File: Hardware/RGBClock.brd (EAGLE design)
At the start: 81.3 x 81.3 mm, 89 parts, among them IC1 PTH08080W, IC2 LP2985-Digital, IC3 LP2985-Analog, IC4 MCP1824S, IC5 PTH08080W, Q1 MS5V, T1 IRF7205, T2 SI2323, T3 PUMH*, X1 NEB21R, X2 MICRO-SD3

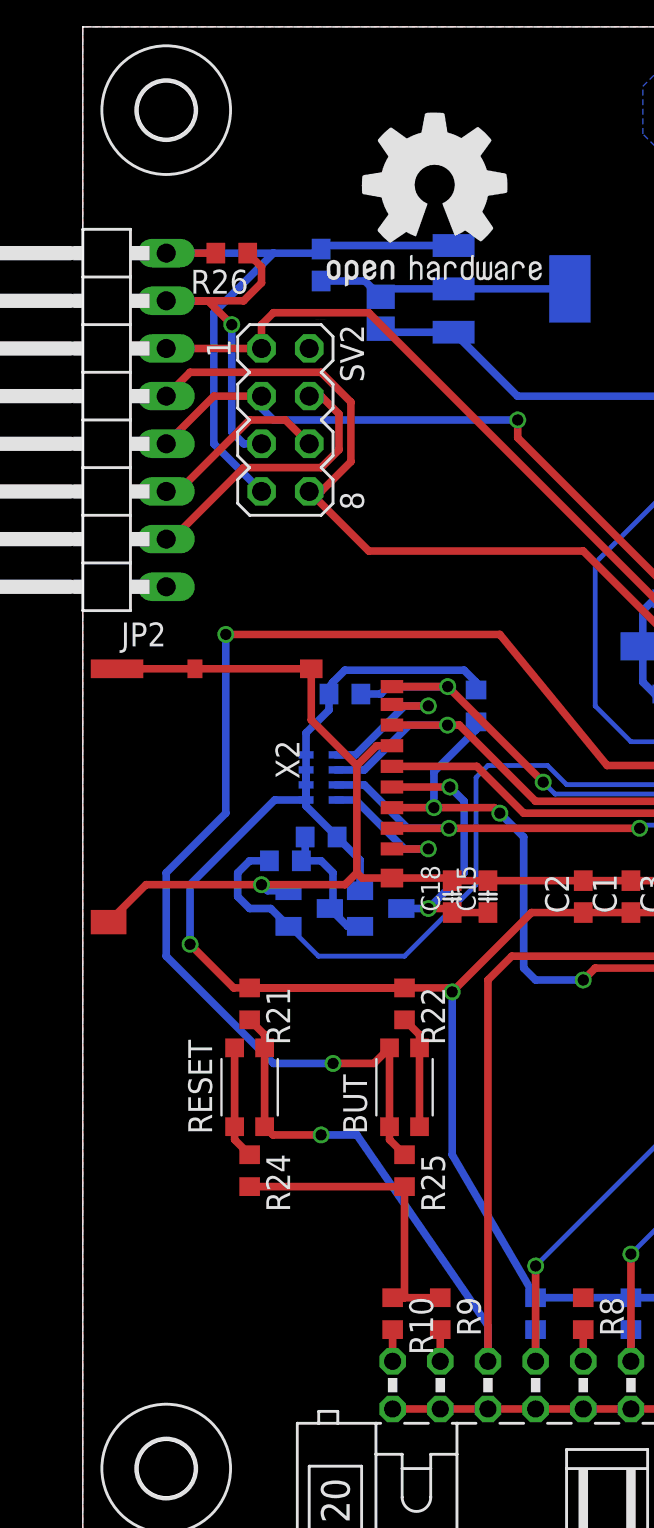
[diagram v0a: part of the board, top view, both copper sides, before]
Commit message: added github url on PCB
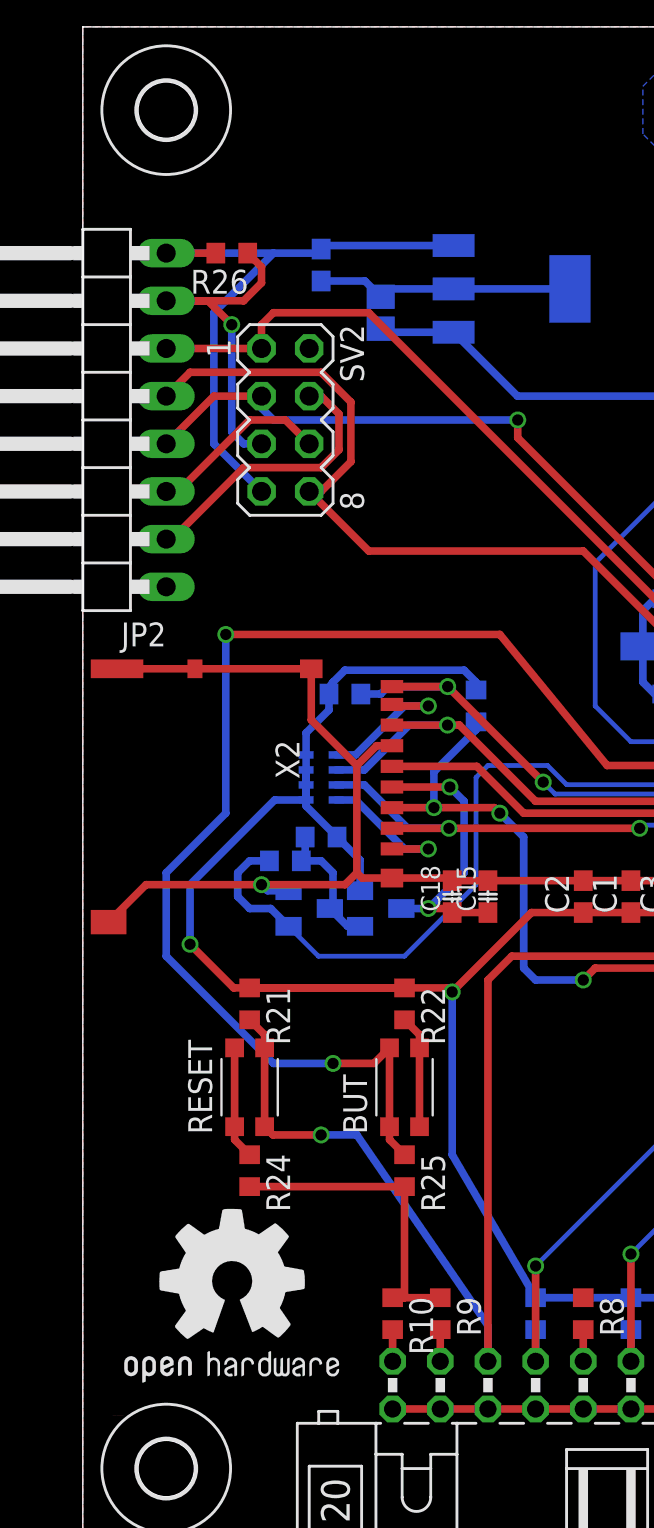
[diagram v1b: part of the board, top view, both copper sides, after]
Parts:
- moved GOLD_ORB_SM1 59.4 mm to (1.59, 7.30)
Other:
- board text added: "https://github.com/matthiasb85/RGB-Clock"
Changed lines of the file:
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@@
 <rectangle x1="6.985" y1="53.34" x2="29.845" y2="67.31" layer="51"/>
 <rectangle x1="53.975" y1="59.69" x2="67.945" y2="76.2" layer="51"/>
-<text x="11.43" y="77.47" size="1.27" layer="51" font="vector" ratio="16" distance="26">RGB Clock v0.1
+<text x="9.2075" y="73.9775" size="1.4224" layer="51" font="vector" ratio="16" distance="26">RGB Clock v0.1
 M.B. 11.2014</text>
+<text x="9.2075" y="72.0725" size="0.6096" layer="51" font="vector" ratio="16" distance="26">https://github.com/matthiasb85/RGB-Clock</text>
 </plain>
 <attributes>
@@
 <attribute name="DIGIKEY-PN" value="513-1457-1-ND" x="36.83" y="59.69" size="1.778" layer="27" rot="R270" display="off"/>
 </element>
-<element name="GOLD_ORB_SM1" library="bfl" package="OSHW1" value="OSHWLOGO_GOLD_ORB_MED" x="12.3825" y="65.7225"/>
+<element name="GOLD_ORB_SM1" library="bfl" package="OSHW1" value="OSHWLOGO_GOLD_ORB_MED" x="1.5875" y="7.3025"/>
 <element name="JP6" library="pinhead" package="1X14/90" value="" x="80.645" y="53.34" rot="R270"/>
 <element name="JP1" library="pinhead" package="1X03/90" value="" x="40.64" y="80.645"/>

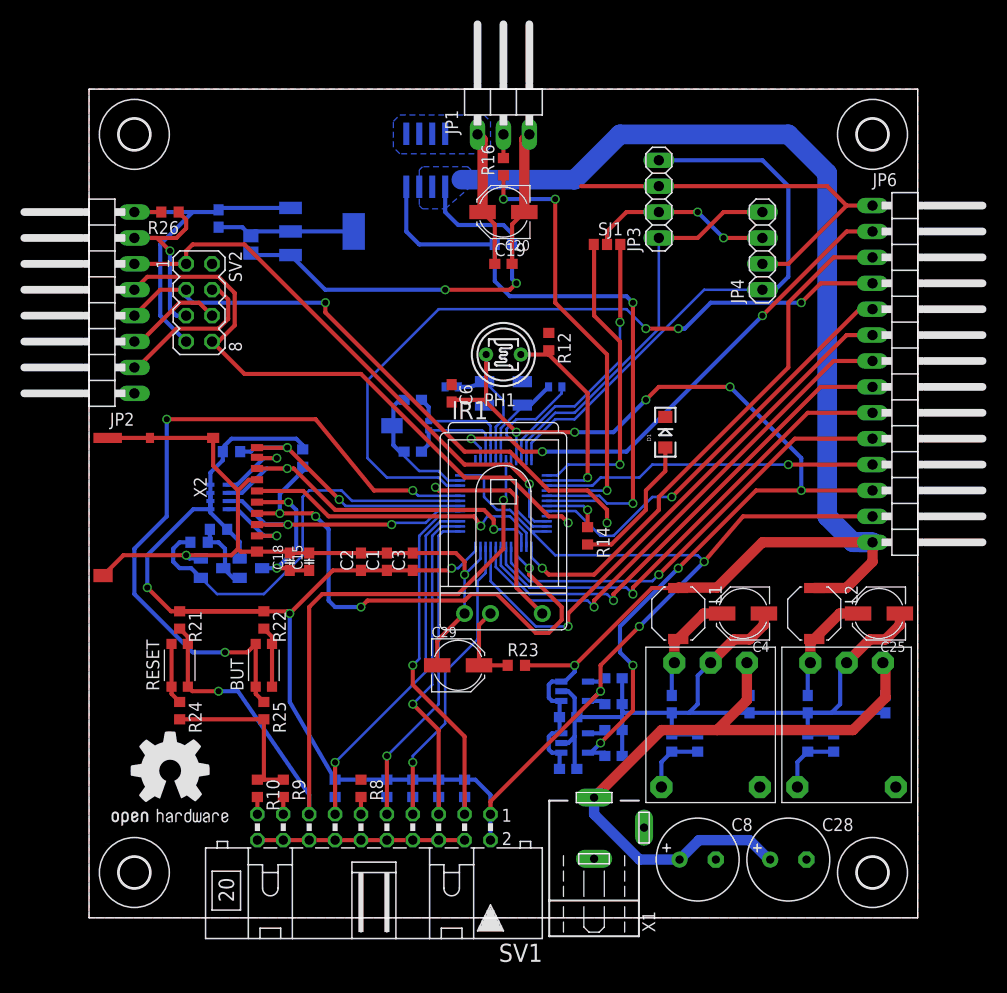
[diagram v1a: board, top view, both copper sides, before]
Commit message: worked on board worked on silkscreen -> first version should be ready within a few commits
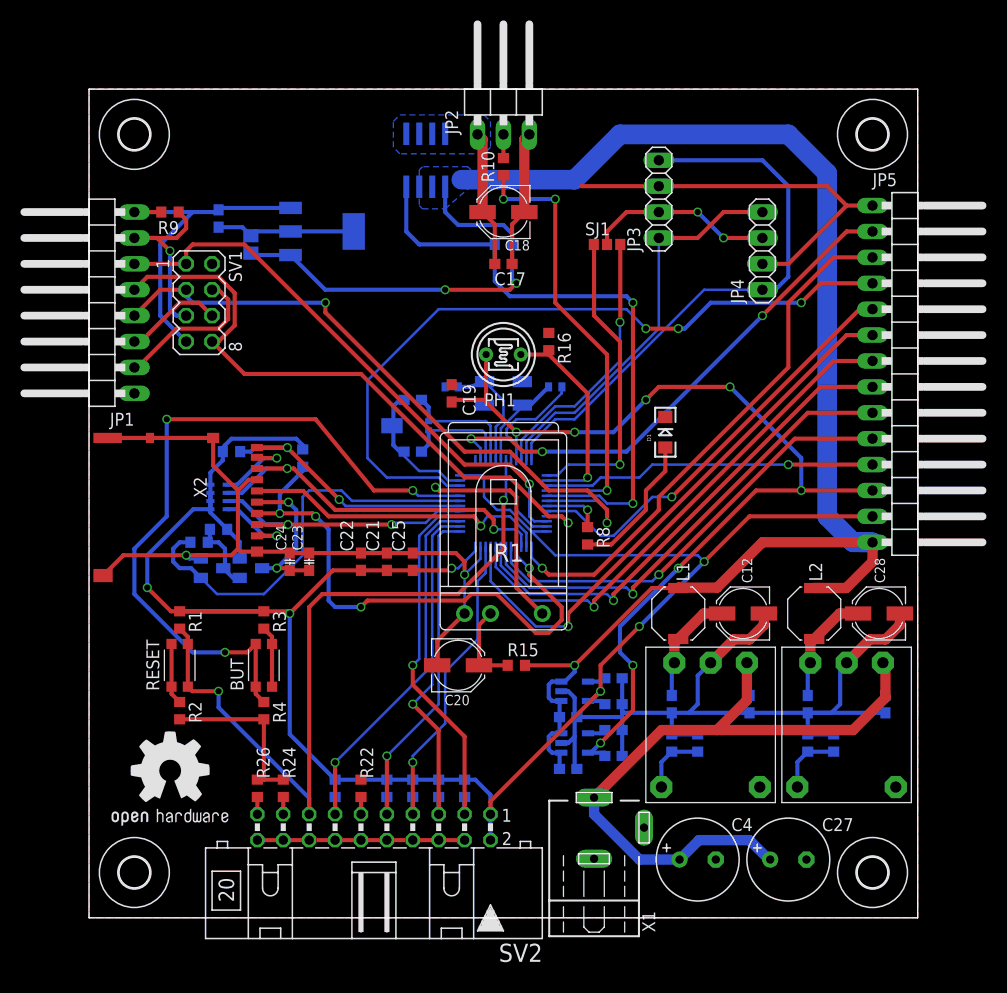
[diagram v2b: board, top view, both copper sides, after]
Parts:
- C1: value 1uF -> 18pF; device rcl:C0603 -> SparkFun:C0402
- C10: value 2u2/16V -> 10n
- C12: value 4,7u/10V -> 100µ/6V3; device 00ralf:C0603-DASHES -> rcl:PANASONIC_C
- C14: value 10n -> 2u2/16V
- C15: value 10u/6V3 -> 2µ2/16V; device 00ralf:C0603-DASHES -> rcl:C0603
- C16: value 10µ/16V -> 100n; device rcl:C0805 -> rcl:C0603
- C17: value 2µ2/16V -> 100n
- C18: value 100n -> 100µ/6V3; device 00ralf:C0603-DASHES -> rcl:PANASONIC_C
- C19: value 100n -> 1uF
- C2: value 1uF -> 100n
- C21, C22: value 18pF -> 1uF; device SparkFun:C0402 -> rcl:C0603
- C23: value 12p -> 10u/6V3; device rcl:C0603 -> 00ralf:C0603-DASHES
- C24: value 12p -> 100n; device rcl:C0603 -> 00ralf:C0603-DASHES
- C25: value 100µ/6V3 -> 12p; device rcl:PANASONIC_C -> rcl:C0603
- C27: value 100n -> 220µ; device rcl:C0603 -> rcl:E3,5-8
- C28: value 220µ -> 100µ/6V3; device rcl:E3,5-8 -> rcl:PANASONIC_C
- C29: value 100µ/6V3 -> 100n; device rcl:PANASONIC_C -> rcl:C0603
- C3: value 12p -> 18pF; device rcl:C0603 -> SparkFun:C0402
- C4: value 100µ/6V3 -> 220µ; device rcl:PANASONIC_C -> rcl:E3,5-8
- C5: value 100n -> 12p
- C6: value 1uF -> 4,7u/10V; device rcl:C0603 -> 00ralf:C0603-DASHES
- C7: value 100n -> 4,7u/10V; device rcl:C0603 -> 00ralf:C0603-DASHES
- C8: value 220µ -> 12p; device rcl:E3,5-8 -> rcl:C0603
- C9: value 4,7u/10V -> 10µ/16V; device 00ralf:C0603-DASHES -> rcl:C0805
- JP1: device pinhead:1X03/90 -> pinhead:1X08/90
- JP2: device pinhead:1X08/90 -> pinhead:1X03/90
- R10: value 10k -> 120
- R11: value 100k -> 22k; device rcl:R0603 -> 00ralf:R0603-DASHES
- R12: value 220k -> 22k; device rcl:R0603 -> 00ralf:R0603-DASHES
- R14: value 1k -> *; device rcl:R0603 -> 00ralf:R0603-DASHES
- R15: value * -> 330; device 00ralf:R0603-DASHES -> rcl:R0603
- R16: value 120 -> 220k
- R17: value 22k -> 180; device 00ralf:R0603-DASHES -> rcl:R0603
- R18: value 22k -> 330; device 00ralf:R0603-DASHES -> rcl:R0603
- R19: value 180 -> 10k
- R2, R3, R8: value 10k -> 1k
- R20, R23: value 330 -> 10k
- R22, R24: value 1k -> 10k
- R5: value 10k -> 100k
- SV1: device con-harting-ml:ML20L -> con-lstb:MA04-2
- SV2: device con-lstb:MA04-2 -> con-harting-ml:ML20L
- T2: value SI2323 -> PUMH*; device transistor-fet:SOT23 -> transistor-digital:SOT23
- T3: value PUMH* -> SI2323; device transistor-digital:SOT23 -> transistor-fet:SOT23
- moved R10 65.6 mm to (40.6, 73.7), turned to 90 degrees
- moved R18 63.3 mm to (70.5, 17.1), turned to 90 degrees
- moved C16 61.1 mm to (57.1, 21.0), turned to 270 degrees
- moved R17 59.1 mm to (73.0, 17.1)
- moved R9 57.6 mm to (7.94, 69.2), turned to 180 degrees
- moved R26 57.2 mm to (16.5, 12.7), turned to 270 degrees
- moved C9 55.8 mm to (15.9, 66.0), turned to 90 degrees
- moved SV1 54.2 mm to (10.8, 60.3), turned to 270 degrees
- moved SV2 54.2 mm to (27.9, 8.89), turned to 180 degrees
- moved R5 53.5 mm to (40.6, 66.0), turned to 180 degrees
- moved R19 49.1 mm to (24.1, 12.7), turned to 270 degrees
- moved C8 48.8 mm to (31.8, 45.7), flipped to the bottom
- moved C25 46.0 mm to (31.8, 34.9), turned to 90 degrees
- moved JP1 44.9 mm to (0.64, 60.3), turned to 90 degrees
- moved JP2 44.9 mm to (40.6, 80.6), turned to 0 degrees
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- renumbered JP6 to JP5
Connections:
- net +12V: now also C2.1, C26.1, C27.+, C4.+; no longer C27.1, C28.+, C7.1, C8.+
- net +3V3: now also C13.1, C21.1, C22.1, C25.1, R11.2, R12.2, R19.1, R20.1, R23.1, R25.1, SV2.1, SV2.2, T3.2; no longer C1.1, C10.1, C2.1, C3.1, R17.2, R18.2, R2.1, R22.1, R4.1, R5.1, SV1.1, SV1.2, T2.2
- net +3V3/ANALOG: now also C14.1, C19.2; no longer C13.1, C6.2
- net +5V5: now also C6.1, C7.1, R15.2, R5.2; no longer C12.1, C16.1, R11.2, R23.2
- net +6V_EXT: now also C12.+, C16.1; no longer C4.+, C5.1
- net +6V_EXT1: now also C28.+, C29.1; no longer C25.+, C26.1
- net BOOT0: now also R4.1; no longer R25.1
- net ESP_3V3: now also C15.1, JP1.8, R9.2, SV1.7; no longer C17.1, JP2.8, R26.2, SV2.7
- net ESP_GPIO0: now also JP1.3, SV1.6; no longer JP2.3, SV2.6
- net ESP_GPIO2: now also JP1.2, SV1.4; no longer JP2.2, SV2.4
- net ESP_PD: now also JP1.4, SV1.3; no longer JP2.4, SV2.3
- net ESP_RES: now also JP1.7, R9.1, SV1.5; no longer JP2.7, R26.1, SV2.5
- net ESP_RX: now also JP1.5, SV1.8; no longer JP2.5, SV2.8
- net ESP_TX: now also JP1.6, SV1.1; no longer JP2.6, SV2.1
- net GND: now also C12.-, C18.-, C19.1, C25.2, C27.-, C29.2, C6.2, C8.2, JP1.1, JP2.3, R16.1, R17.2, R18.2, R2.2, R22.1, R24.1, R26.1, R4.2, SV1.2, SV2.10, SV2.12, SV2.14, SV2.16, SV2.18, SV2.20, SV2.4, SV2.6, SV2.8, T2.2; no longer C12.2, C18.2, C19.2, C25.-, C27.2, C29.-, C6.1, C8.-, JP1.3, JP2.1, R10.1, R12.1, R19.2, R20.2, R24.2, R25.2, R8.1, R9.1, SV1.10, SV1.12, SV1.14, SV1.16, SV1.18, SV1.20, SV1.4, SV1.6, SV1.8, SV2.2, T3.2
- net LED: now also R8.1; no longer R14.1
- net LIGHT_AIN: now also R16.2; no longer R12.2
- net LP2985_BYPASS: now also C11.1; no longer C14.1
- net LP2985_BYPASS1: now also C10.1; no longer C11.1
- net N$1: now also R3.2; no longer R22.2
- net N$10: now also C20.+, R15.1; no longer C29.+, R23.1
- net N$2: now also R8.2; no longer R14.2
- net N$3: now also JP2.2, R10.2; no longer JP1.2, R16.2
- net N$4: now also R2.1; no longer R24.1
- net N$5: now also R17.1, R18.1; no longer R19.1, R20.1
- net N$6: now also R26.2, SV2.19; no longer R10.2, SV1.19
- net N$8: now also R24.2, SV2.17; no longer R9.2, SV1.17
- net N$9: now also R22.2, SV2.11; no longer R8.2, SV1.11
- net OSC32_IN: now also C8.1; no longer C24.1
- net OSC32_OUT: now also C5.1; no longer C23.1
- net OSC_IN: now also C3.1; no longer C22.1
- net OSC_OUT: now also C1.1; no longer C21.1
- net RESET: now also R1.2, SV2.15; no longer R21.2, SV1.15
- net SDIO_VCC: now also C23.1, C24.1, T3.3; no longer C15.1, C18.1, T2.3
- net SD_MOSI: now also R12.1; no longer R17.1
- net SD_PWR: now also R14.2, T2.1; no longer R15.2, T3.1
- net SD_PWR_INV: now also R14.1, T2.3, T3.1; no longer R15.1, T2.1, T3.3
- net SD_SWITCH: now also R11.1; no longer R18.1
- net TCK: now also R20.2, SV2.9; no longer R2.2, SV1.9
- net TDI: now also R23.2, SV2.5; no longer R4.2, SV1.5
- net TDO: now also R19.2, SV2.13; no longer R1.2, SV1.13
- net TMS: now also R21.2, SV2.7; no longer R3.2, SV1.7
- net TRST: now also R25.2, SV2.3; no longer R5.2, SV1.3
- net WS_DATA: now also R10.1; no longer R16.1
- net WS_ENA: now also R5.1; no longer R11.1
- net WS_SUPPLY: now also C17.1, C18.+, JP2.1; no longer C19.1, C20.+, JP1.1

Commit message: minor changes on board and schematic
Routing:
- net ESP_3V3: vias 1 -> 0
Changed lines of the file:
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@@
 <layers>
 <layer number="1" name="Top" color="4" fill="1" visible="yes" active="yes"/>
-<layer number="16" name="Bottom" color="1" fill="1" visible="no" active="yes"/>
+<layer number="16" name="Bottom" color="1" fill="1" visible="yes" active="yes"/>
 <layer number="17" name="Pads" color="2" fill="1" visible="yes" active="yes"/>
 <layer number="18" name="Vias" color="2" fill="1" visible="yes" active="yes"/>
@@
 <layer number="20" name="Dimension" color="15" fill="1" visible="yes" active="yes"/>
 <layer number="21" name="tPlace" color="7" fill="1" visible="yes" active="yes"/>
-<layer number="22" name="bPlace" color="7" fill="1" visible="no" active="yes"/>
+<layer number="22" name="bPlace" color="7" fill="1" visible="yes" active="yes"/>
 <layer number="23" name="tOrigins" color="15" fill="1" visible="yes" active="yes"/>
-<layer number="24" name="bOrigins" color="15" fill="1" visible="no" active="yes"/>
+<layer number="24" name="bOrigins" color="15" fill="1" visible="yes" active="yes"/>
 <layer number="25" name="tNames" color="7" fill="1" visible="yes" active="yes"/>
-<layer number="26" name="bNames" color="7" fill="1" visible="no" active="yes"/>
+<layer number="26" name="bNames" color="7" fill="1" visible="yes" active="yes"/>
 <layer number="27" name="tValues" color="7" fill="1" visible="no" active="yes"/>
 <layer number="28" name="bValues" color="7" fill="1" visible="no" active="yes"/>
@@
 <layer number="50" name="dxf" color="7" fill="1" visible="no" active="no"/>
 <layer number="51" name="tDocu" color="7" fill="1" visible="yes" active="yes"/>
-<layer number="52" name="bDocu" color="7" fill="1" visible="no" active="yes"/>
+<layer number="52" name="bDocu" color="7" fill="1" visible="yes" active="yes"/>
 <layer number="53" name="tGND_GNDA" color="7" fill="9" visible="no" active="no"/>
 <layer number="54" name="bGND_GNDA" color="1" fill="9" visible="no" active="no"/>
@@
 <rectangle x1="6.985" y1="53.34" x2="29.845" y2="67.31" layer="51"/>
 <rectangle x1="53.975" y1="59.69" x2="67.945" y2="76.2" layer="51"/>
-<text x="11.7475" y="72.7075" size="1.4224" layer="51" font="vector" ratio="16" distance="26">RGB Clock v0.1
+<text x="10.16" y="73.66" size="1.778" layer="51" font="vector" ratio="16" distance="26">RGB Clock v0.1
 M.B. 11.2014</text>
-<text x="11.7475" y="71.12" size="0.6096" layer="51" font="vector" ratio="16" distance="26">https://github.com/matthiasb85/RGB-Clock</text>
+<text x="10.16" y="71.755" size="0.8128" layer="51" font="vector" ratio="16" distance="26">https://github.com/matthiasb85/RGB-Clock</text>
 </plain>
 <attributes>
@@
 <attribute name="VALUE" x="39.751" y="62.103" size="1.27" layer="27"/>
 </element>
-<element name="SV2" library="con-harting-ml" package="ML20L" value="" x="27.94" y="8.89" rot="R180">
+<element name="SV2" library="con-harting-ml" package="ML20L" value="" x="27.94" y="8.89" smashed="yes" rot="R180">
 <attribute name="OC_NEWARK" value="unknown" x="-17.78" y="11.43" size="1.778" layer="27" rot="R180" display="off"/>
 <attribute name="MPN" value="" x="-17.78" y="11.43" size="1.778" layer="27" rot="R180" display="off"/>
 <attribute name="MF" value="" x="-17.78" y="11.43" size="1.778" layer="27" rot="R180" display="off"/>
 <attribute name="OC_FARNELL" value="unknown" x="-17.78" y="11.43" size="1.778" layer="27" rot="R180" display="off"/>
+<attribute name="NAME" x="41.5925" y="12.4079" size="1.778" layer="25" ratio="10" rot="R270"/>
+<attribute name="VALUE" x="33.0454" y="-2.54" size="1.778" layer="27" ratio="10" rot="R180"/>
 </element>
 <element name="R20" library="rcl" package="R0603" value="10k" x="29.21" y="12.7" smashed="yes" rot="MR270">
@@
 <element name="H3" library="holes" package="3,0" value="MOUNT-HOLE3.0" x="4.445" y="76.835"/>
 <element name="H4" library="holes" package="3,0" value="MOUNT-HOLE3.0" x="76.835" y="76.835"/>
-<element name="X1" library="con-lumberg" package="NEB21R" value="NEB21R" x="49.53" y="4.445">
+<element name="X1" library="con-lumberg" package="NEB21R" value="NEB21R" x="49.53" y="4.445" smashed="yes">
 <attribute name="OC_NEWARK" value="97K6458" x="49.53" y="4.445" size="1.778" layer="27" display="off"/>
 <attribute name="MPN" value="NEB 21 R" x="49.53" y="4.445" size="1.778" layer="27" display="off"/>
 <attribute name="MF" value="" x="49.53" y="4.445" size="1.778" layer="27" display="off"/>
 <attribute name="OC_FARNELL" value="1217037" x="49.53" y="4.445" size="1.778" layer="27" display="off"/>
+<attribute name="NAME" x="55.53" y="1.77" size="1.27" layer="25" rot="R90"/>
+<attribute name="VALUE" x="44.53" y="-1.405" size="1.27" layer="27" rot="R90"/>
 </element>
 <element name="IC4" library="linear" package="SOT223" value="MCP1824S" x="22.86" y="67.31" rot="MR90"/>
@@
 <contactref element="R9" pad="2"/>
 <contactref element="JP1" pad="8"/>
-<wire x1="7.0875" y1="69.215" x2="4.445" y2="69.215" width="0.4064" layer="1"/>
-<via x="4.445" y="69.215" extent="1-16" drill="0.6" shape="square"/>
-<wire x1="4.445" y1="69.215" x2="10.16" y2="69.215" width="0.4064" layer="16"/>
 <wire x1="10.16" y1="69.215" x2="12.485" y2="69.215" width="0.4064" layer="16"/>
 <wire x1="12.485" y1="69.215" x2="12.7" y2="69.43" width="0.4064" layer="16"/>
+<wire x1="4.445" y1="69.215" x2="10.16" y2="69.215" width="0.4064" layer="16"/>
+<wire x1="7.0875" y1="69.215" x2="4.445" y2="69.215" width="0.4064" layer="1"/>
 </signal>
 <signal name="N$5">

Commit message: modified board, better placement for C21,22,25
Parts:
- moved C22 6.35 mm to (33.0, 34.9), flipped to the bottom, turned to 270 degrees
- moved C21 5.40 mm to (34.6, 34.9), flipped to the bottom, turned to 270 degrees
- moved C25 4.45 mm to (36.2, 34.9), flipped to the bottom, turned to 270 degrees
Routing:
- net +3V3: track 202.9 -> 192.5 mm
- net GND: track 298.9 -> 288.6 mm, vias 2 -> 1
- net TRST: track 36.2 -> 39.6 mm
- net TDI: track 34.0 -> 36.4 mm
- net TDO: track 36.6 -> 37.8 mm
- net TCK: track 33.4 -> 34.5 mm
